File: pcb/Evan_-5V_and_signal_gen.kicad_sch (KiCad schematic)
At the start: 34 parts, among them IC1 TL7660IDGKR, IC2 TL081IDT, IC4 UA78M33CDCYG3, U2 LTC4300A-1IMS8_PBF, U5 TPS2069CDBVR_MOSFET

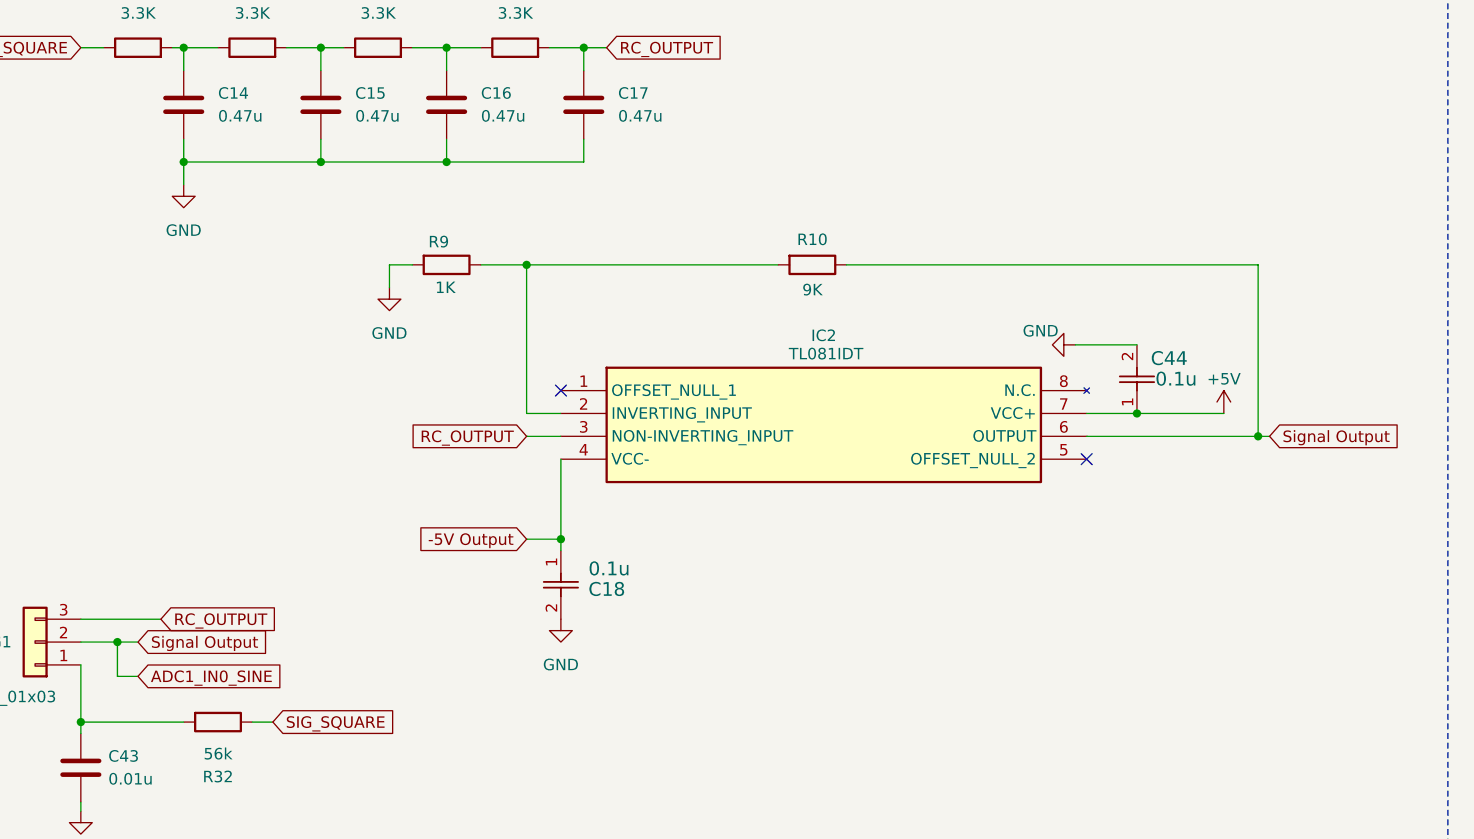
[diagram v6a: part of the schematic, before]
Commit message: Added capacitor to op amp circuit
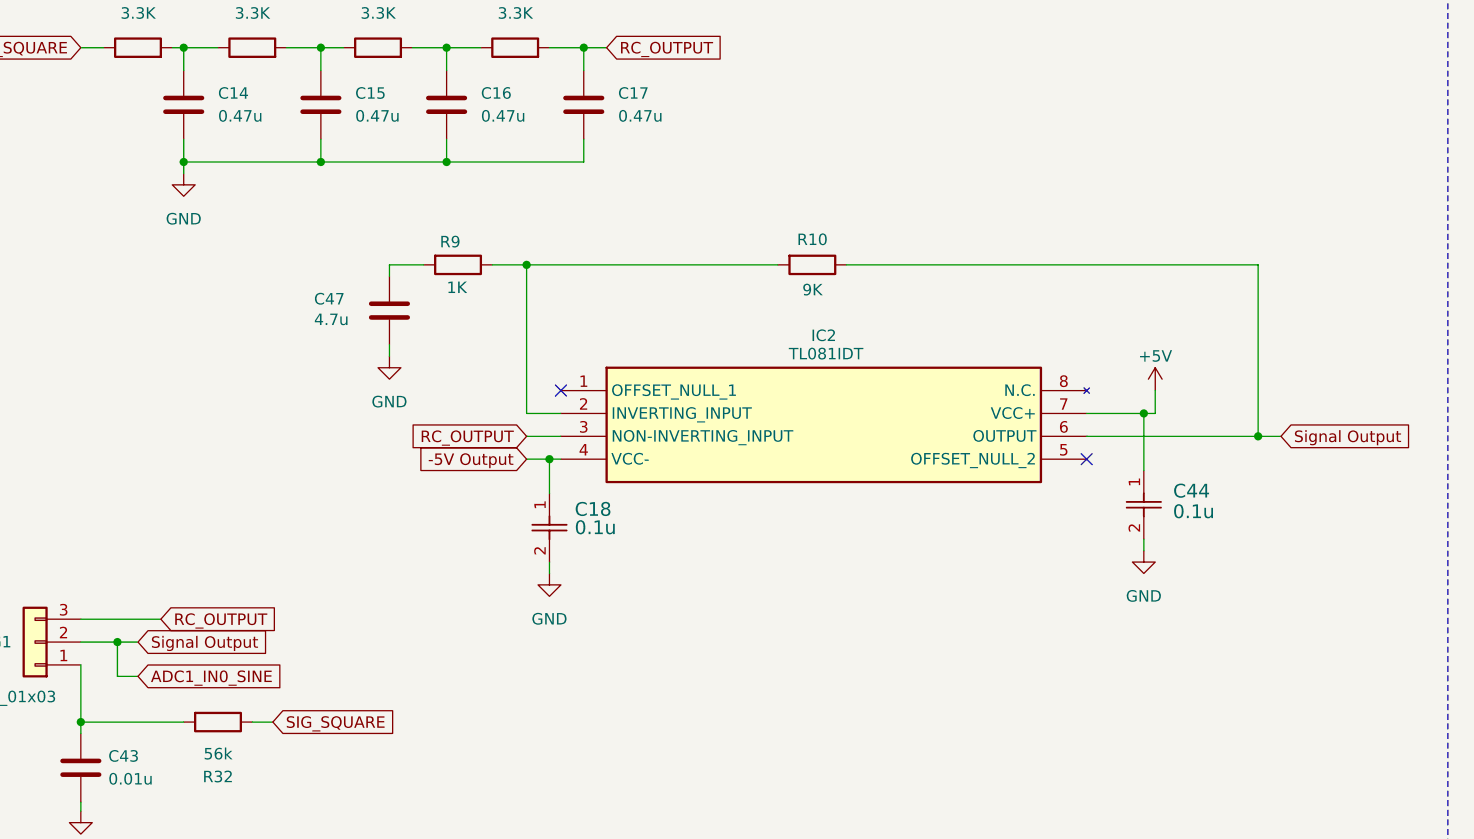
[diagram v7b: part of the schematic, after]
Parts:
- added C47: 4.7u, Capacitor_SMD:C_0805_2012Metric, symbol Device:C
- C14, C15, C16, C17, C18: footprint capstone:CAPC220145_88N_KEM-0.1u -> Capacitor_SMD:C_0805_2012Metric
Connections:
- net GND: now also C47.2; no longer R9.2
- new net: C47.1, R9.2
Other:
- moved on the sheet: C18, C44, R9

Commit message: Added switchable input for opto-coupler
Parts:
- C14, C15, C16, C17, C47: footprint Capacitor_SMD:C_0805_2012Metric -> Capacitor_SMD:C_0402_1005Metric
- C43: footprint capstone:C0805 -> Capacitor_SMD:C_0402_1005Metric
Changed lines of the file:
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@@
 			)
 		)
-		(property "Footprint" "Capacitor_SMD:C_0805_2012Metric"
+		(property "Footprint" "Capacitor_SMD:C_0402_1005Metric"
 			(at 167.3352 58.42 0)
 			(effects
@@
 			)
 		)
-		(property "Footprint" "Capacitor_SMD:C_0805_2012Metric"
+		(property "Footprint" "Capacitor_SMD:C_0402_1005Metric"
 			(at 159.7152 35.56 0)
 			(effects
@@
 			)
 		)
-		(property "Footprint" "Capacitor_SMD:C_0805_2012Metric"
+		(property "Footprint" "Capacitor_SMD:C_0402_1005Metric"
 			(at 188.9252 35.56 0)
 			(effects
@@
 			)
 		)
-		(property "Footprint" "Capacitor_SMD:C_0805_2012Metric"
+		(property "Footprint" "Capacitor_SMD:C_0402_1005Metric"
 			(at 173.6852 35.56 0)
 			(effects
@@
 			)
 		)
-		(property "Footprint" "Capacitor_SMD:C_0805_2012Metric"
+		(property "Footprint" "Capacitor_SMD:C_0402_1005Metric"
 			(at 144.4752 35.56 0)
 			(effects
@@
 			)
 		)
-		(property "Footprint" "capstone:C0805"
+		(property "Footprint" "Capacitor_SMD:C_0402_1005Metric"
 			(at 131.1148 101.6 0)
 			(effects
